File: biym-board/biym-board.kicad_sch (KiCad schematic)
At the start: 1 part

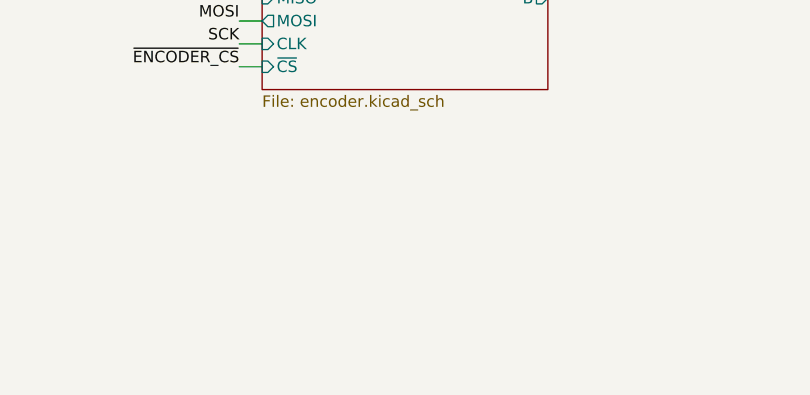
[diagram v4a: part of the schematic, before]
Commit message: Add led sheet
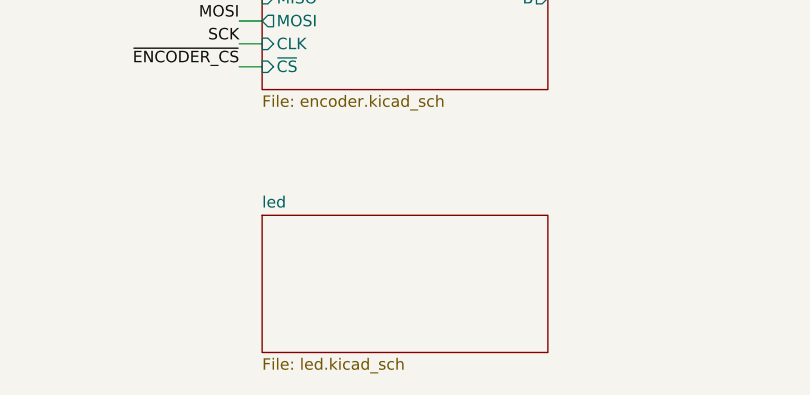
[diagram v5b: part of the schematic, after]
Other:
- added sheet led (led.kicad_sch)
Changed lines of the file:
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@@
+    )
+  )
+  (sheet (at 166.37 137.16) (size 31.75 15.24) (fields_autoplaced)
+    (stroke (width 0.1524) (type solid) (color 0 0 0 0))
+    (fill (color 0 0 0 0.0000))
+    (property "Sheet name" "led" (id 0) (at 166.37 136.4484 0)
+      (effects (font (size 1.27 1.27)) (justify left bottom))
+    )
+    (property "Sheet file" "led.kicad_sch" (id 1) (at 166.37 152.9846 0)
+      (effects (font (size 1.27 1.27)) (justify left top))
     )
   )
@@
     (path "/79116d11-26fd-48fc-b8f9-7a7b774125a1" (page "3"))
     (path "/63981df2-6365-426b-91a2-0a3730bf331a" (page "4"))
+    (path "/ba7902c8-ef45-407b-94b0-d9c747cdabc9" (page "5"))
   )
   (symbol_instances

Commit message: Wire led sheet
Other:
- sheet led ports: added CKI, GND, SDI, VLED; removed none
- moved on the sheet: FW1

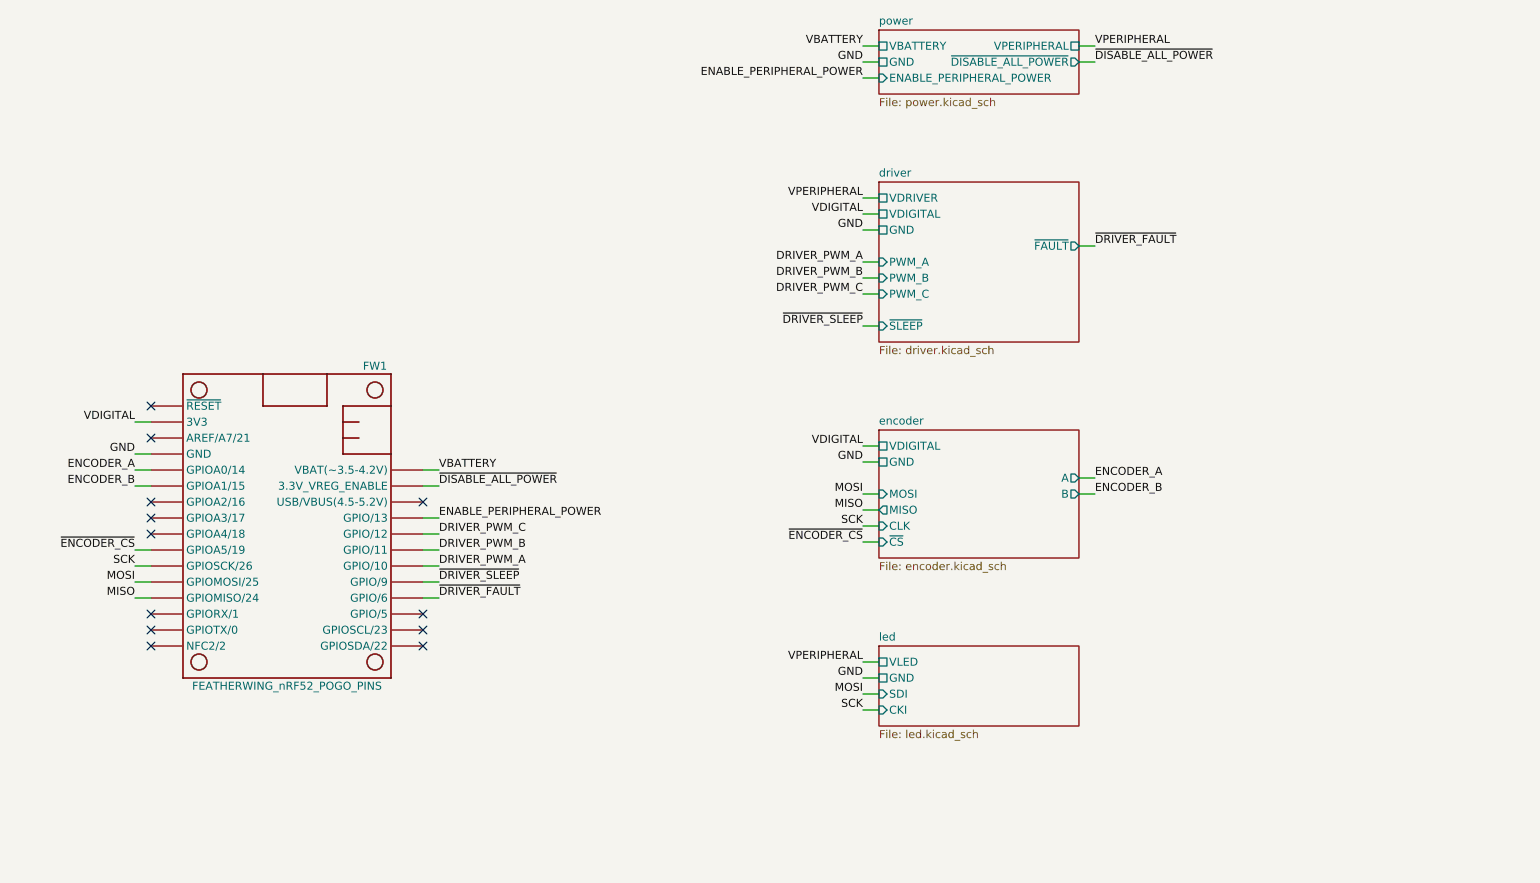
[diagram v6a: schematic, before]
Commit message: Add boosted voltage
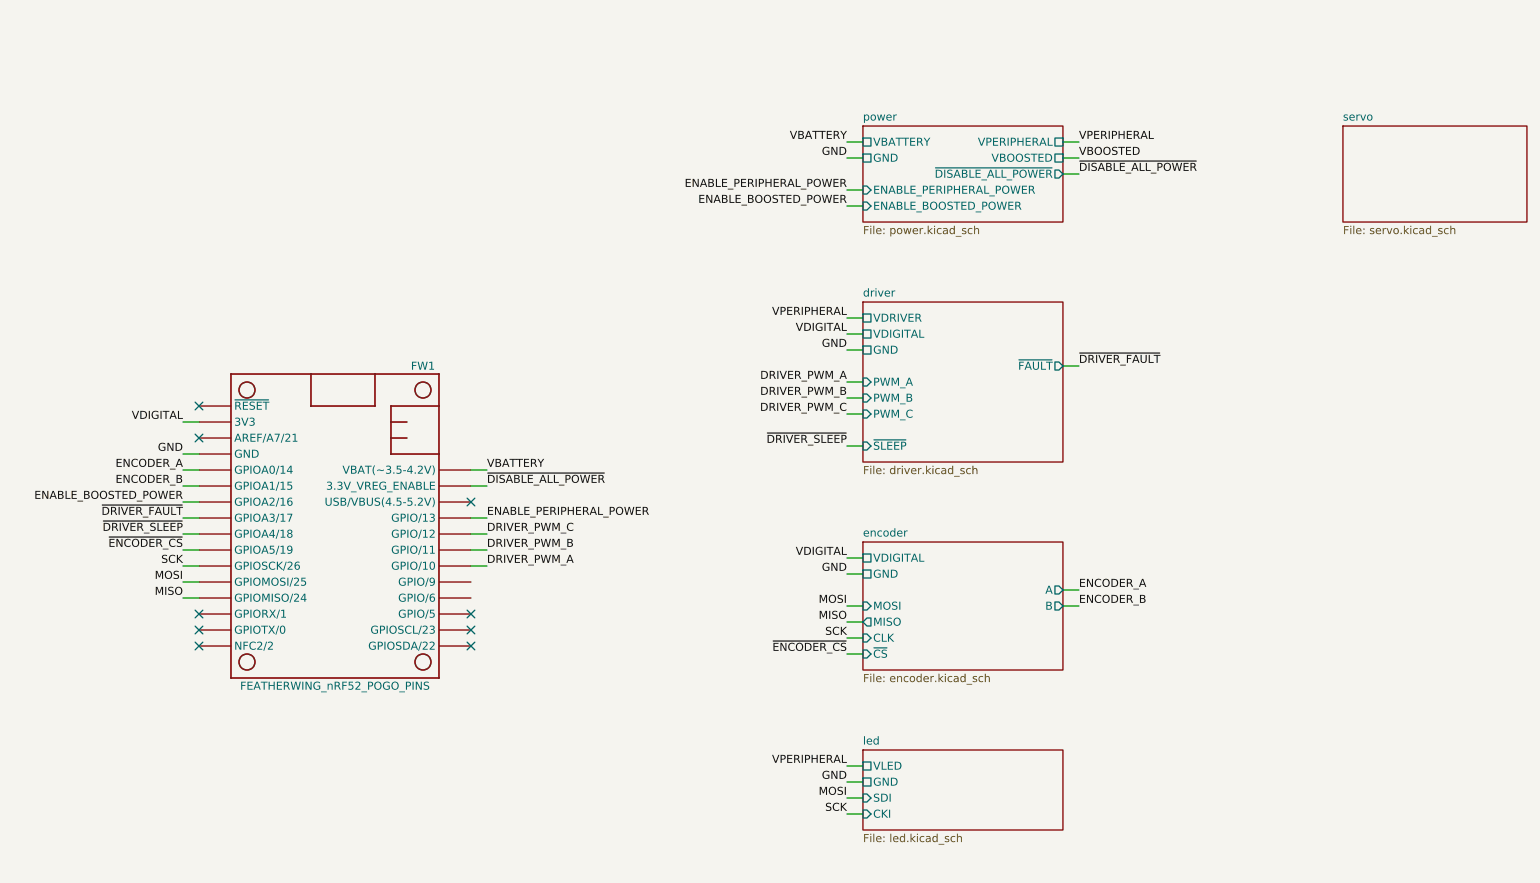
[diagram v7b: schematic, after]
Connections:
- net ~{DRIVER_FAULT}: now also FW1.8 (GPIOA3/17); no longer FW1.20 (GPIO/6)
- net ~{DRIVER_SLEEP}: now also FW1.9 (GPIOA4/18); no longer FW1.21 (GPIO/9)
- net ENABLE_BOOSTED_POWER: now reaches FW1.7 (GPIOA2/16)
- no-connect marks 12 -> 9
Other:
- added sheet servo (servo.kicad_sch)
- sheet power ports: added ENABLE_BOOSTED_POWER, VBOOSTED; removed none
- moved on the sheet: FW1

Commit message: servo -> output
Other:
- sheet servo renamed output
- sheet output: file servo.kicad_sch -> output.kicad_sch
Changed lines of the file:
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@@
     (stroke (width 0.1524) (type solid) (color 0 0 0 0))
     (fill (color 0 0 0 0.0000))
-    (property "Sheet name" "servo" (id 0) (at 224.79 36.1184 0)
+    (property "Sheet name" "output" (id 0) (at 224.79 36.1184 0)
       (effects (font (size 1.27 1.27)) (justify left bottom))
     )
-    (property "Sheet file" "servo.kicad_sch" (id 1) (at 224.79 52.6546 0)
+    (property "Sheet file" "output.kicad_sch" (id 1) (at 224.79 52.6546 0)
       (effects (font (size 1.27 1.27)) (justify left top))
     )
